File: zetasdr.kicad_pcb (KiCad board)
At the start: 2 copper layers, 77.5 x 43.5 mm, 47 parts, among them J2 USB_B, J5 Antenna, J6 AudioJack3_SwitchTR, Q1 BC547C, U1 74AHC1G04, U2 74HC74, U3 4052, U4 NE5532

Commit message: first layout
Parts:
- removed J6: AudioJack3_SwitchTR, Connector_Audio:Jack_3.5mm_CUI_SJ1-3525N_Horizontal
- removed R10, R9: 4k7, Resistor_SMD:R_0805_2012Metric_Pad1.20x1.40mm_HandSolder
- removed RV1: 50k, Potentiometer_THT:Potentiometer_Piher_T-16H_Single_Horizontal
- added H3: MountingHole_Pad, MountingHole:MountingHole_3.2mm_M3_Pad, F.Cu at (165.0, 138.6)
- added J1: Output I, Connector_Coaxial:SMA_Amphenol_901-143_Horizontal, F.Cu at (221.2, 80.0)
- added J3: Output Q, Connector_Coaxial:SMA_Amphenol_901-143_Horizontal, F.Cu at (221.0, 100.0)
- added J4: Input AWG, Connector_Coaxial:SMA_Amphenol_901-143_Horizontal, F.Cu at (221.0, 120.0)
- C1, C13, C14, C15, C17, C18, C2, C3, C4, C9, D2, J5, L1, R7, R8, U1: moved to F.Cu
- moved H2 135.2 mm to (219.5, 60.3)
- moved H4 132.8 mm to (219.0, 139.8)
- moved C7 109.0 mm to (209.5, 83.0), turned to 180 degrees
- moved R4 107.9 mm to (214.5, 83.0), turned to 180 degrees
- moved U4 101.9 mm to (214.5, 86.2), turned to -90 degrees
- moved C10 100.2 mm to (207.0, 80.2), turned to 0 degrees
- moved C5 99.2 mm to (204.0, 88.2)
- moved R1 99.2 mm to (209.6, 128.2), turned to 180 degrees
- moved C6 98.9 mm to (204.0, 91.8)
- moved C8 98.3 mm to (207.0, 97.2), turned to 180 degrees
- moved R11 96.8 mm to (185.7, 138.3), turned to 180 degrees
- moved Q1 92.2 mm to (209.6, 124.0), turned to 180 degrees
- moved U1 90.5 mm to (208.5, 131.5), turned to 0 degrees
- moved U2 86.4 mm to (194.7, 115.8), turned to -90 degrees
- moved TP1 86.2 mm to (213.0, 76.8)
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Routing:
- net Net-(U3-X2): track 85.7 -> 36.3 mm, vias 0 -> 1
- net Net-(U3-X0): track 81.2 -> 48.4 mm
- net Net-(U3-X3): track 41.5 -> 69.6 mm, vias 0 -> 1
- net Net-(U3-X1): track 61.6 -> 35.2 mm
- net Net-(U2A-C): track 12.2 -> 38.3 mm, vias 0 -> 1
- net VCC: track 147.5 -> 172.8 mm, vias 0 -> 1
- net GND: track 23.4 -> 0.00 mm, vias 2 -> 0
- net Net-(C10-Pad2): track 33.3 -> 17.6 mm
- net Net-(U2A-D): track 34.7 -> 23.0 mm
- net Net-(J5-In): track 18.2 -> 7.12 mm, vias 1 -> 0
- net Net-(U2A-~{Q}): track 32.2 -> 21.9 mm
- net Net-(Q1-E): track 10.1 -> 17.5 mm
- net Net-(C12-Pad2): track 21.2 -> 15.0 mm
- net Net-(R10-Pad1): track 3.34 -> 0.00 mm
- net Net-(J4-In): track 6.64 -> 9.20 mm
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- removed copper zone on B.Cu, net GND
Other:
- board size 77.5 x 43.5 mm -> 68 x 92 mm

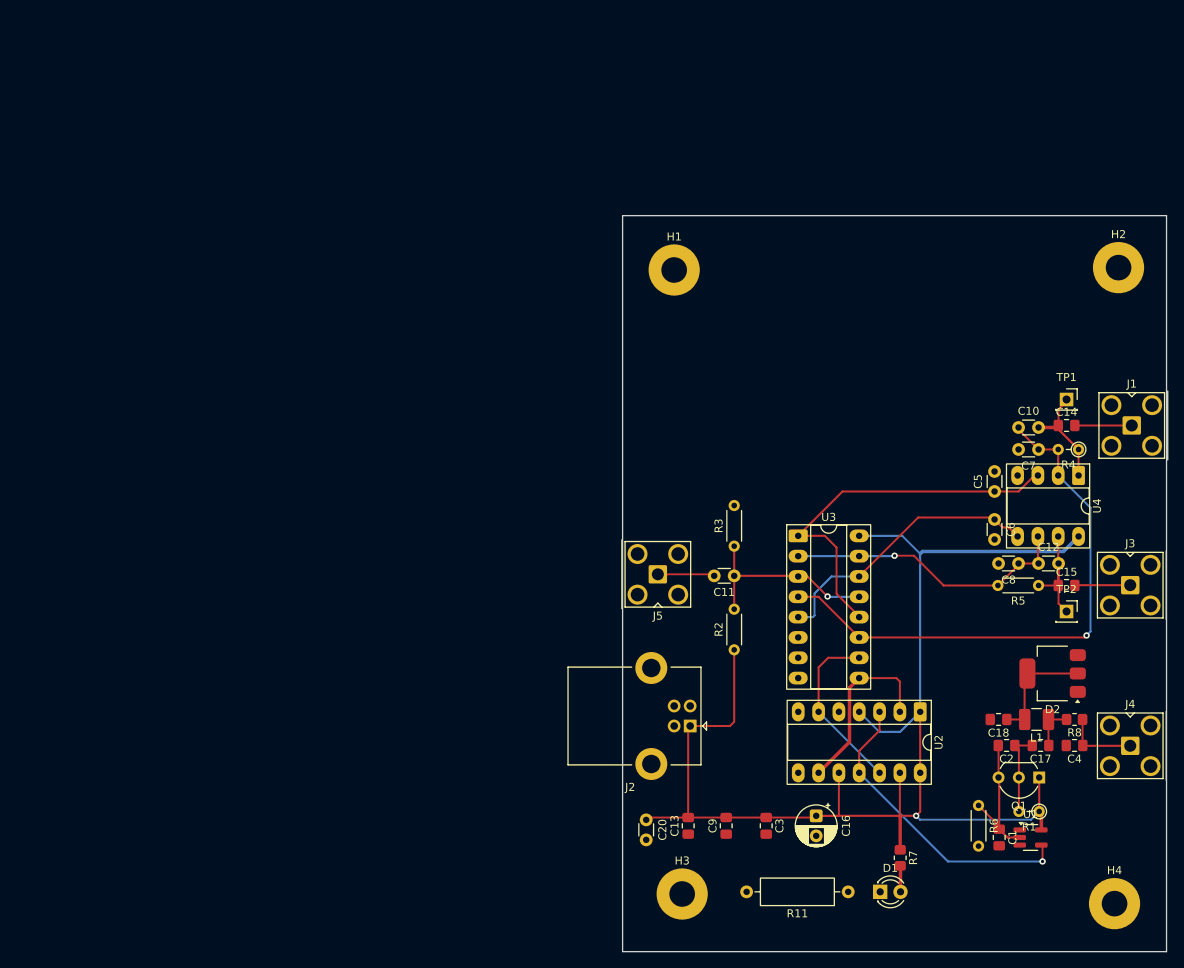
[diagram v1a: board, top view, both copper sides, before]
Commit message: 80m filter & new layout
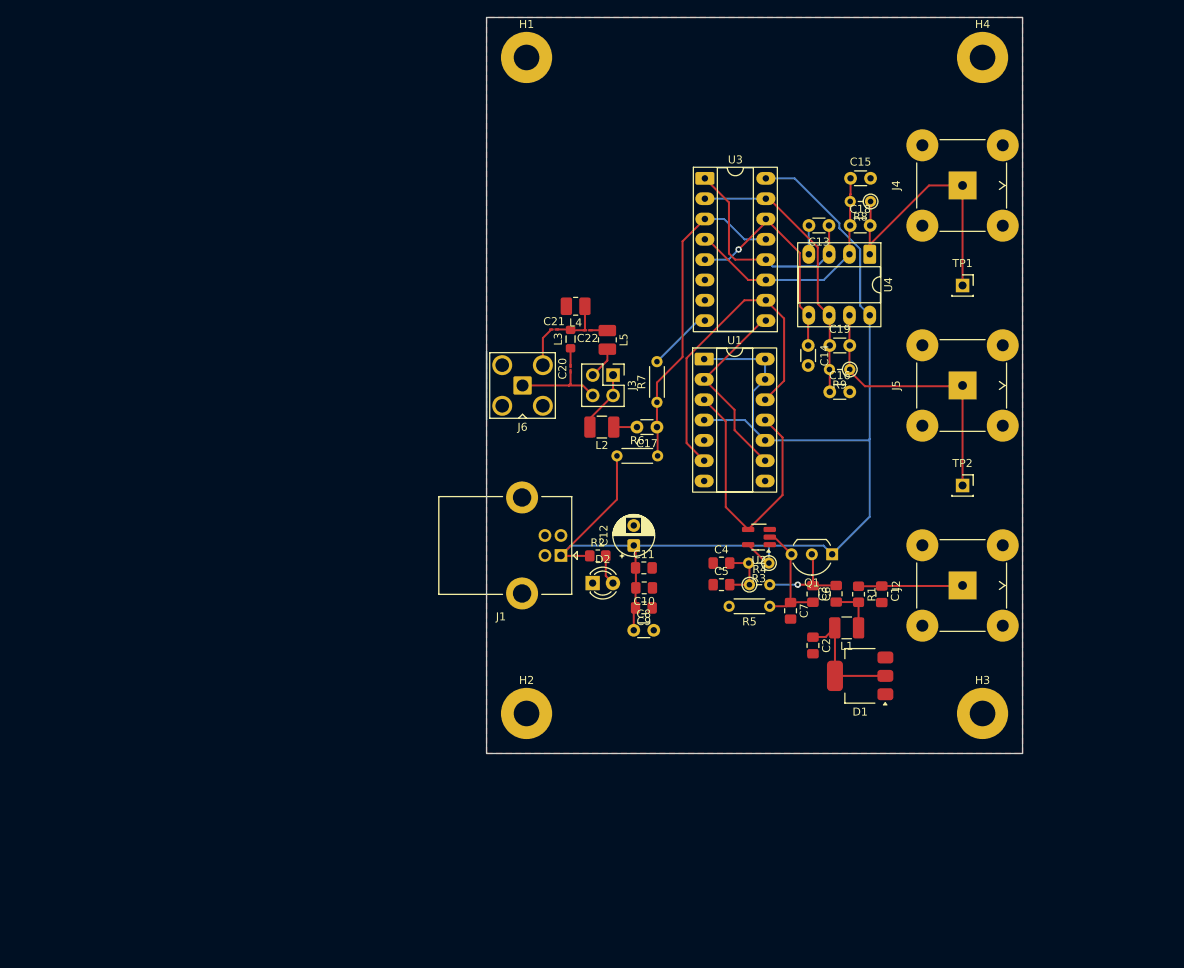
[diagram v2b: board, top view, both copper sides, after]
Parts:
- removed R11: 0, Resistor_THT:R_Axial_DIN0309_L9.0mm_D3.2mm_P12.70mm_Horizontal
- added C19: 330p, Capacitor_THT:C_Disc_D3.0mm_W1.6mm_P2.50mm, F.Cu at (183.4, 70.0)
- added C21: 10n, Capacitor_SMD:C_01005_0402Metric_Pad0.57x0.30mm_HandSolder, F.Cu at (148.9, 68.0)
- added C22: 150p, Capacitor_SMD:C_01005_0402Metric_Pad0.57x0.30mm_HandSolder, F.Cu at (153.1, 68.1)
- added J6: Antenna, Connector_Coaxial:SMA_Amphenol_901-143_Horizontal, F.Cu at (145.0, 75.0)
- added L2: 6.8u, Inductor_SMD:L_1210_3225Metric_Pad1.42x2.65mm_HandSolder, F.Cu at (154.9, 80.2)
- added L3: 27u, Inductor_SMD:L_0805_2012Metric_Pad1.05x1.20mm_HandSolder, F.Cu at (151.0, 69.2)
- added L4: 180n, Inductor_SMD:L_1008_2520Metric_Pad1.43x2.20mm_HandSolder, F.Cu at (151.6, 65.1)
- added L5: 12u, Inductor_SMD:L_1008_2520Metric_Pad1.43x2.20mm_HandSolder, F.Cu at (155.6, 69.3)
- added R9: 5k1, Resistor_THT:R_Axial_DIN0204_L3.6mm_D1.6mm_P2.54mm_Vertical, F.Cu at (185.9, 73.0)
- C1: value 82p -> 100n
- C10, C11: value 330p -> 100n; footprint Capacitor_THT:C_Disc_D3.0mm_W1.6mm_P2.50mm -> Capacitor_SMD:C_0805_2012Metric_Pad1.18x1.45mm_HandSolder
- C12: value 330p -> 10u; footprint Capacitor_THT:C_Disc_D3.0mm_W1.6mm_P2.50mm -> Capacitor_THT:CP_Radial_D5.0mm_P2.50mm
- C13: value 100n -> 22n; footprint Capacitor_SMD:C_0805_2012Metric_Pad1.18x1.45mm_HandSolder -> Capacitor_THT:C_Disc_D3.0mm_W1.6mm_P2.50mm
- C14, C15: value 2u2 -> 22n; footprint Capacitor_SMD:C_0805_2012Metric_Pad1.18x1.45mm_HandSolder -> Capacitor_THT:C_Disc_D3.0mm_W1.6mm_P2.50mm
- C16: value 10u -> 22n; footprint Capacitor_THT:CP_Radial_D5.0mm_P2.50mm -> Capacitor_THT:C_Disc_D3.0mm_W1.6mm_P2.50mm
- C17: value 100n -> 330p; footprint Capacitor_SMD:C_0805_2012Metric_Pad1.18x1.45mm_HandSolder -> Capacitor_THT:C_Disc_D3.0mm_W1.6mm_P2.50mm
- C18: value DNP -> 330p; footprint Capacitor_SMD:C_0805_2012Metric_Pad1.18x1.45mm_HandSolder -> Capacitor_THT:C_Disc_D3.0mm_W1.6mm_P2.50mm
- C2: value 82p -> DNP
- C20: value 100n -> 68p; footprint Capacitor_THT:C_Disc_D3.0mm_W1.6mm_P2.50mm -> Capacitor_SMD:C_01005_0402Metric_Pad0.57x0.30mm_HandSolder
- C5: value 22n -> 1u; footprint Capacitor_THT:C_Disc_D3.0mm_W1.6mm_P2.50mm -> Capacitor_SMD:C_0805_2012Metric_Pad1.18x1.45mm_HandSolder
- C6, C7: value 22n -> 82p; footprint Capacitor_THT:C_Disc_D3.0mm_W1.6mm_P2.50mm -> Capacitor_SMD:C_0805_2012Metric_Pad1.18x1.45mm_HandSolder
- C8: value 22n -> 100n
- D1: value LED -> mv7404; footprint LED_THT:LED_D3.0mm -> Package_TO_SOT_SMD:SOT-223-3_TabPin2
- D2: value mv7404 -> LED; footprint Package_TO_SOT_SMD:SOT-223-3_TabPin2 -> LED_THT:LED_D3.0mm
- J1: value Output I -> USB_B; footprint Connector_Coaxial:SMA_Amphenol_901-143_Horizontal -> Connector_USB:USB_B_Lumberg_2411_02_Horizontal
- J2: value USB_B -> Input AWG; footprint Connector_USB:USB_B_Lumberg_2411_02_Horizontal -> Connector_Coaxial:BNC_TEConnectivity_1478035_Horizontal
- J3: value Output Q -> Conn_02x02_Counter_Clockwise; footprint Connector_Coaxial:SMA_Amphenol_901-143_Horizontal -> Connector_PinHeader_2.54mm:PinHeader_2x02_P2.54mm_Vertical
- J4: value Input AWG -> Output I; footprint Connector_Coaxial:SMA_Amphenol_901-143_Horizontal -> Connector_Coaxial:BNC_TEConnectivity_1478035_Horizontal
- J5: value Antenna -> Output Q; footprint Connector_Coaxial:SMA_Amphenol_901-143_Horizontal -> Connector_Coaxial:BNC_TEConnectivity_1478035_Horizontal
- R1: footprint Resistor_THT:R_Axial_DIN0204_L3.6mm_D1.6mm_P2.54mm_Vertical -> Resistor_SMD:R_0805_2012Metric_Pad1.20x1.40mm_HandSolder
- R2: footprint Resistor_THT:R_Axial_DIN0204_L3.6mm_D1.6mm_P5.08mm_Horizontal -> Resistor_SMD:R_0805_2012Metric_Pad1.20x1.40mm_HandSolder
- R3: value 1k -> 50; footprint Resistor_THT:R_Axial_DIN0204_L3.6mm_D1.6mm_P5.08mm_Horizontal -> Resistor_THT:R_Axial_DIN0204_L3.6mm_D1.6mm_P2.54mm_Vertical
- R4: value 5k1 -> 50
- R5: value 5k1 -> 380
- R6: value 380 -> 1k
- R7: footprint Resistor_SMD:R_0805_2012Metric_Pad1.20x1.40mm_HandSolder -> Resistor_THT:R_Axial_DIN0204_L3.6mm_D1.6mm_P5.08mm_Horizontal
- R8: value 100k -> 5k1; footprint Resistor_SMD:R_0805_2012Metric_Pad1.20x1.40mm_HandSolder -> Resistor_THT:R_Axial_DIN0204_L3.6mm_D1.6mm_P2.54mm_Vertical
- U1: value 74AHC1G04 -> 74HC74; footprint Package_TO_SOT_SMD:SOT-23-5_HandSoldering -> Package_DIP:DIP-14_W7.62mm_Socket_LongPads
- U2: value 74HC74 -> 74AHC1G04; footprint Package_DIP:DIP-14_W7.62mm_Socket_LongPads -> Package_TO_SOT_SMD:SOT-23-5_HandSoldering
- moved H4 107.0 mm to (202.5, 34.0)
- moved H2 92.6 mm to (145.5, 116.0)
- moved C13 77.1 mm to (183.3, 55.0), turned to 180 degrees
- moved J1 73.2 mm to (149.8, 96.2), turned to 180 degrees
- moved J4 73.1 mm to (200.0, 50.0)
- moved U1 72.4 mm to (167.7, 71.7)
- moved J3 69.8 mm to (156.3, 73.7)
- moved R8 69.6 mm to (188.5, 52.0)
- moved R7 64.6 mm to (161.8, 77.1), turned to 90 degrees
- moved C18 64.5 mm to (185.9, 55.0), turned to 0 degrees
- moved R6 62.9 mm to (156.8, 83.8), turned to 0 degrees
- moved C17 62.3 mm to (161.8, 80.2)
- moved D2 58.6 mm to (153.8, 99.7), turned to 0 degrees
- moved C15 57.6 mm to (186.0, 49.1)
- moved C20 57.2 mm to (151.0, 72.9), turned to 90 degrees
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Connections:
- C1 pad 1: Net-(Q1-E) -> Net-(J2-In)
- C10 pad 1: Net-(U3-X3) -> GND
- C10 pad 2: Net-(C10-Pad2) -> VCC
- C11 pad 1: Net-(U3-X) -> VCC
- C11 pad 2: Net-(J5-In) -> GND
- C12 pad 1: Net-(U3-X2) -> VCC
- C12 pad 2: Net-(C12-Pad2) -> GND
- C13 pad 1: GND -> Net-(U3-X0)
- C13 pad 2: VCC -> GND
- C14 pad 1: Net-(C10-Pad2) -> Net-(U3-X1)
- C14 pad 2: Net-(J1-In) -> GND
- C15 pad 1: Net-(C12-Pad2) -> Net-(U3-X3)
- C15 pad 2: Net-(J3-In) -> GND
- C16 pad 1: VCC -> Net-(U3-X2)
- C17 pad 1: Net-(C17-Pad1) -> Net-(U3-X)
- C17 pad 2: Net-(Q1-B) -> Net-(C17-Pad2)
- C18 pad 1: Net-(D2-K) -> Net-(U3-X3)
- C18 pad 2: GND -> Net-(J4-In)
- C2 pad 1: Net-(Q1-B) -> Net-(D1-K)
- C2 pad 2: Net-(Q1-E) -> GND
- C20 pad 1: VCC -> /80m szűrő/Input
- C20 pad 2: GND -> Net-(C20-Pad2)
- C3 pad 1: VCC -> Net-(C3-Pad1)
- C3 pad 2: GND -> Net-(Q1-B)
- C4 pad 1: Net-(J4-In) -> GND
- C4 pad 2: GND -> Net-(C4-Pad2)
- C5 pad 1: Net-(U3-X0) -> GND
- C5 pad 2: GND -> Net-(C4-Pad2)
- C6 pad 1: Net-(U3-X1) -> Net-(Q1-B)
- C6 pad 2: GND -> Net-(Q1-E)
- C7 pad 1: Net-(U3-X3) -> Net-(Q1-E)
- C8 pad 1: Net-(U3-X2) -> VCC
- D1 pad 2: Net-(D1-A) -> Net-(D1-K)
- D2 pad 2: Net-(D2-K) -> Net-(D2-A)
- J1 pad 1: Net-(J1-In) -> VCC
- J1 pad 2: GND -> unconnected-(J1-D--Pad2)
- J2 pad 1: VCC -> Net-(J2-In)
- J2 pad 2: unconnected-(J2-D--Pad2) -> GND
- J3 pad 1: Net-(J3-In) -> Net-(J3-Pin_1)
- J3 pad 2: GND -> Net-(J3-Pin_1)
- L1 pad 1: Net-(C17-Pad1) -> Net-(C3-Pad1)
- L1 pad 2: Net-(D2-K) -> Net-(D1-K)
- R1 pad 1: VCC -> Net-(J2-In)
- R1 pad 2: Net-(Q1-B) -> Net-(C3-Pad1)
- R2 pad 2: Net-(U3-X) -> Net-(D2-A)
- R3 pad 1: Net-(U3-X) -> VCC
- R3 pad 2: GND -> Net-(C4-Pad2)
- R4 pad 1: Net-(C10-Pad2) -> Net-(C4-Pad2)
- R4 pad 2: Net-(U3-X3) -> Net-(Q1-B)
- R5 pad 1: Net-(C12-Pad2) -> Net-(Q1-E)
- R5 pad 2: Net-(U3-X2) -> GND
- R6 pad 1: Net-(Q1-E) -> VCC
- R6 pad 2: GND -> Net-(U3-X)
- R7 pad 1: VCC -> Net-(U3-X)
- R7 pad 2: Net-(D1-A) -> GND
- R8 pad 2: Net-(C17-Pad1) -> Net-(U3-X3)
- TP1 pad 1: Net-(C10-Pad2) -> Net-(J4-In)
- TP2 pad 1: Net-(C12-Pad2) -> Net-(J5-In)
- U1 pad 1: (no net) -> VCC
- U1 pad 2: Net-(Q1-E) -> Net-(U1A-D)
- U1 pad 3: GND -> Net-(U1A-C)
- U1 pad 4: Net-(U2A-C) -> VCC
- U1 pad 5: VCC -> unconnected-(U1A-Q-Pad5)
- U2 pad 1: VCC -> (no net)
- U2 pad 2: Net-(U2A-D) -> Net-(Q1-E)
- U2 pad 3: Net-(U2A-C) -> GND
- U2 pad 4: VCC -> Net-(U1A-C)
- U2 pad 5: unconnected-(U2A-Q-Pad5) -> VCC
- U3 pad 10: Net-(U2A-~{Q}) -> Net-(U1A-~{Q})
- U3 pad 9: Net-(U2A-D) -> Net-(U1A-D)
- U4 pad 1: Net-(C10-Pad2) -> Net-(J4-In)
- U4 pad 7: Net-(C12-Pad2) -> Net-(J5-In)
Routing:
- net Net-(U1A-~{Q}): track 0.00 -> 41.0 mm
- net Net-(U3-X3): track 69.6 -> 31.1 mm, vias 1 -> 0
- net Net-(U2A-C): track 38.3 -> 0.00 mm, vias 1 -> 0
- net Net-(U1A-C): track 0.00 -> 34.9 mm
- net Net-(J5-In): track 7.12 -> 34.6 mm
- net Net-(J4-In): track 9.20 -> 35.0 mm
- net Net-(U1A-D): track 0.00 -> 24.1 mm
- net Net-(U2A-D): track 23.0 -> 0.00 mm
- net Net-(U2A-~{Q}): track 21.9 -> 0.00 mm
- net Net-(U3-X0): track 48.4 -> 28.1 mm
- net Net-(C10-Pad2): track 17.6 -> 0.00 mm
- net GND: track 0.00 -> 16.6 mm
- net Net-(U3-X): track 25.3 -> 40.8 mm, vias 1 -> 0
- net Net-(D1-K): track 0.00 -> 15.5 mm
- net Net-(C12-Pad2): track 15.0 -> 0.00 mm
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- added copper zone on F.Cu, net GND
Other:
- board size 68 x 92 mm -> 67 x 92 mm

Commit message: bom
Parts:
- removed L2: 6.8u, Inductor_SMD:L_1210_3225Metric_Pad1.42x2.65mm_HandSolder
- C17: value 330p -> 1n
- C20, C21, C22: footprint Capacitor_SMD:C_01005_0402Metric_Pad0.57x0.30mm_HandSolder -> Capacitor_SMD:C_0603_1608Metric_Pad1.08x0.95mm_HandSolder
- C8: footprint Capacitor_THT:C_Disc_D3.0mm_W1.6mm_P2.50mm -> Capacitor_SMD:C_0805_2012Metric_Pad1.18x1.45mm_HandSolder
- J2, J4, J5: footprint Connector_Coaxial:BNC_TEConnectivity_1478035_Horizontal -> Connector_Coaxial:BNC_Amphenol_B6252HB-NPP3G-50_Horizontal
- L4, L5: footprint Inductor_SMD:L_1008_2520Metric_Pad1.43x2.20mm_HandSolder -> Inductor_SMD:L_0805_2012Metric_Pad1.15x1.40mm_HandSolder
- R3, R4: value 50 -> 50k
- R5: value 380 -> 380 (383)
- U2: footprint Package_TO_SOT_SMD:SOT-23-5_HandSoldering -> Package_TO_SOT_SMD:SOT-353_SC-70-5_Handsoldering
- moved J2 5.00 mm to (195.0, 100.0)
- moved J4 5.00 mm to (195.0, 50.0)
- moved J5 5.00 mm to (195.0, 75.0)
- moved C2 4.03 mm to (179.8, 111.2)
- moved U2 2.76 mm to (172.2, 92.5)
- moved L5 1.80 mm to (157.4, 69.4)
- moved C8 1.30 mm to (160.2, 105.6)
- moved D2 1.22 mm to (153.6, 100.9)
- moved C21 1.20 mm to (147.7, 68.0)
- moved C22 0.76 mm to (153.9, 68.1)
- moved C20 0.44 mm to (151.0, 73.3)
- moved C18 0.25 mm to (186.2, 55.0)
- moved C15 0.20 mm to (186.2, 49.1)
- moved R8 0.20 mm to (188.7, 52.0)
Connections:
- C17 pad 2: Net-(C17-Pad2) -> Net-(J3-Pin_1)
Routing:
- net VCC: track 165.5 -> 220.2 mm
- net Net-(J4-In): track 35.0 -> 28.5 mm
- net Net-(J2-In): track 13.0 -> 8.04 mm
- net Net-(D1-K): track 15.5 -> 19.0 mm
- net Net-(J5-In): track 34.6 -> 31.6 mm
- net Net-(C17-Pad2): track 2.98 -> 0.00 mm
- net Net-(Q1-E): track 15.2 -> 18.2 mm
- net Net-(U1A-~{Q}): track 41.0 -> 42.6 mm
- net GND: track 16.6 -> 17.8 mm, vias 0 -> 1
- net Net-(C21-Pad2): track 6.64 -> 7.77 mm
- net Net-(D2-A): track 3.77 -> 4.89 mm
- net /80m szűrő/Input: track 11.1 -> 10.1 mm
- net /80m szűrő/Output: track 4.08 -> 5.03 mm
- net Net-(C22-Pad1): track 2.14 -> 2.84 mm
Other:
- board text added: "I"
- board text added: "Q"
- board text added: "T"

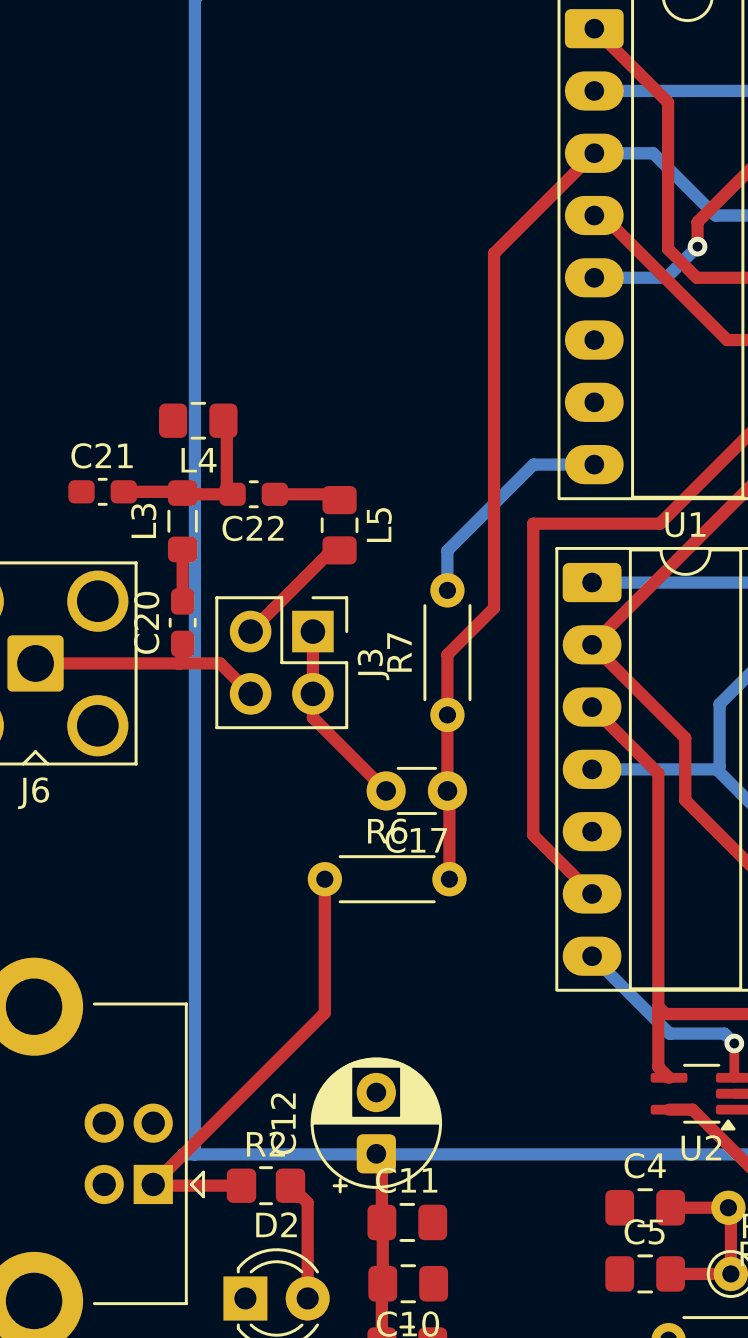
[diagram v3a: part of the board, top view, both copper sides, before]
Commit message: rf bias filtering
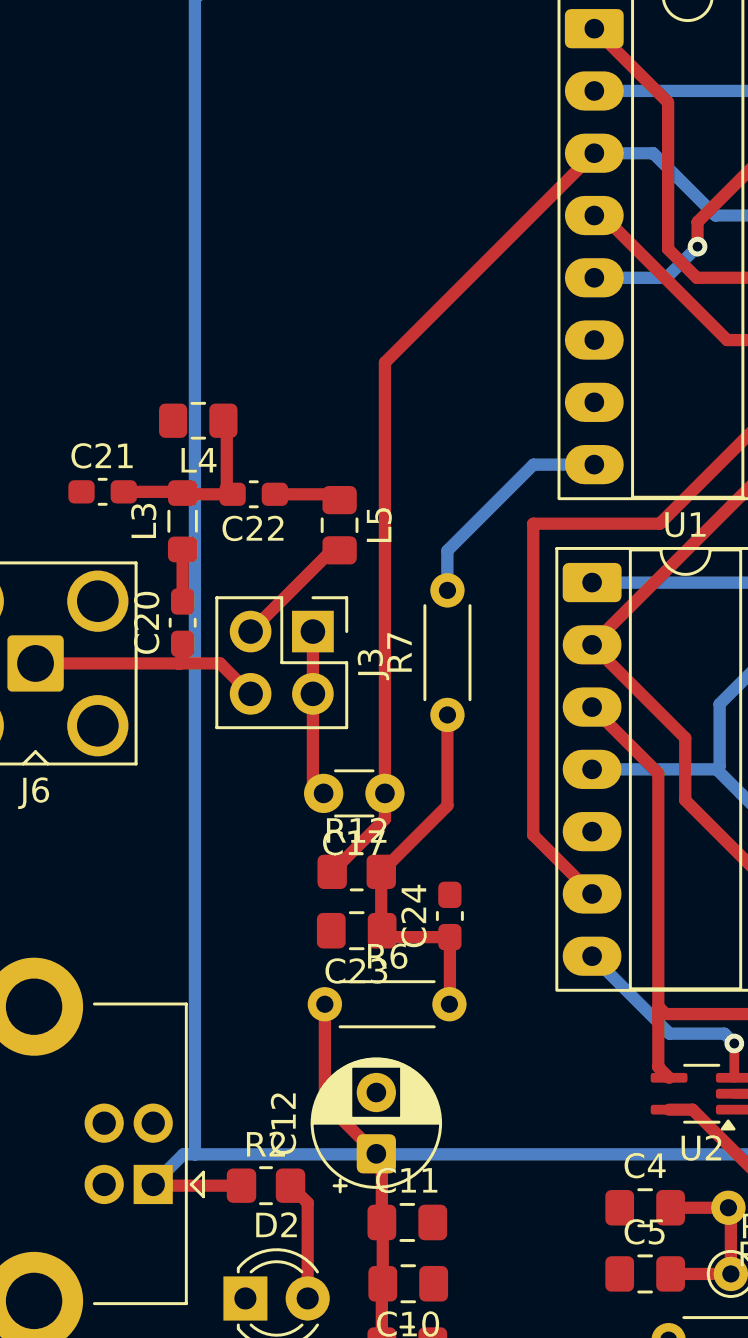
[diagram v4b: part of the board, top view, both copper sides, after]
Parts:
- added C23: 100n, Capacitor_SMD:C_0805_2012Metric_Pad1.18x1.45mm_HandSolder, F.Cu at (158.1, 85.9)
- added C24: 10n, Capacitor_SMD:C_0603_1608Metric_Pad1.08x0.95mm_HandSolder, F.Cu at (161.9, 85.3)
- added R12: 100k, Resistor_SMD:R_0805_2012Metric_Pad1.20x1.40mm_HandSolder, F.Cu at (158.1, 83.5)
- moved R6 5.10 mm to (156.8, 88.9)
- moved C17 2.55 mm to (159.2, 80.3)
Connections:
- R6 pad 2: Net-(U3-X) -> Net-(C23-Pad1)
- R7 pad 1: Net-(U3-X) -> Net-(C23-Pad1)
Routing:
- net Net-(C23-Pad1): track 0.00 -> 15.8 mm
- net VCC: track 220.2 -> 211.8 mm
- net Net-(U3-X): track 40.8 -> 42.4 mm
- net Net-(J3-Pin_1): track 7.74 -> 6.83 mm

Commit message: bias tee
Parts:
- added C25: 10n, Capacitor_SMD:C_0603_1608Metric_Pad1.08x0.95mm_HandSolder, F.Cu at (145.9, 50.7)
- added J7: Conn_02x02_Counter_Clockwise, Connector_PinHeader_2.54mm:PinHeader_2x02_P2.54mm_Vertical, F.Cu at (156.7, 54.0)
- added J8: Conn_02x02_Counter_Clockwise, Connector_PinHeader_2.54mm:PinHeader_2x02_P2.54mm_Vertical, F.Cu at (145.0, 53.9)
- added L2: 22u, Inductor_THT:L_Axial_L9.5mm_D4.0mm_P12.70mm_Horizontal_Fastron_SMCC, F.Cu at (157.2, 46.9)
- moved C20 5.08 mm to (150.6, 68.3)
- moved J3 5.08 mm to (155.9, 68.6)
- moved L3 5.08 mm to (150.6, 64.1)
- moved L5 5.08 mm to (157.0, 64.3)
- moved C22 5.08 mm to (153.5, 63.0)
- moved L4 5.08 mm to (151.2, 60.0)
- moved C21 4.13 mm to (148.2, 63.9), turned to 90 degrees
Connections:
- J6 pad 1: /80m szűrő/Input -> Net-(J6-In)
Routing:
- net Net-(J6-In): track 0.00 -> 30.5 mm
- net /80m szűrő/Input: track 10.1 -> 22.5 mm
- net Net-(J7-Pin_1): track 0.00 -> 7.31 mm
- net Net-(J3-Pin_1): track 6.83 -> 12.6 mm
- net Net-(J8-Pin_2): track 0.00 -> 3.56 mm
- net VCC: track 211.8 -> 214.6 mm
